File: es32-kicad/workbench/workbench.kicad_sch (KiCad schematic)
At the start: 67 parts, among them J1 GND|+5, J10 Rotary Encoder, J11 A[7..0], J2 [9..16], J3 B[0..7], J4 [17..24], J5 Conn_01x03_Socket, J6 Conn_01x03_Socket, J8 Conn_01x06_Socket, J9 [8..0]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

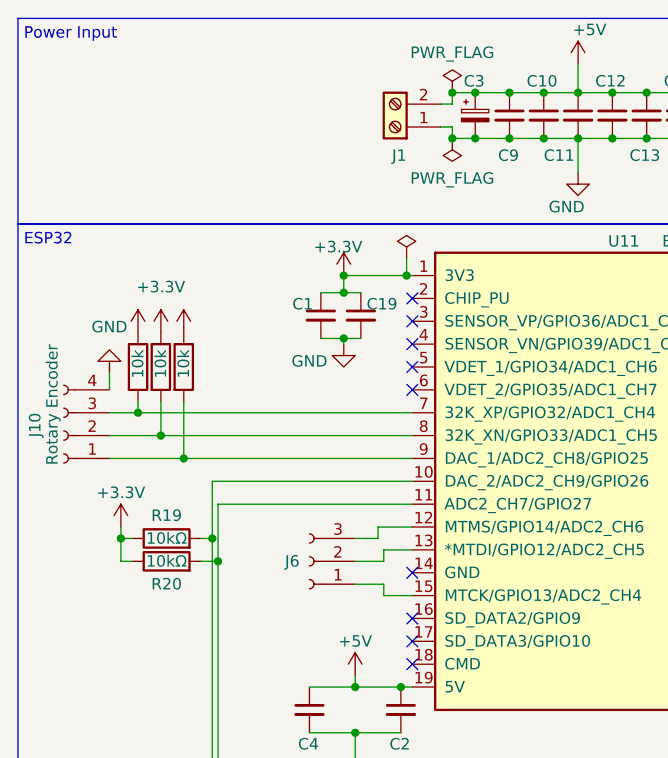
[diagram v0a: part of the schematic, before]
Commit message: adding pins for Leds. Silkscreen. logos. production files
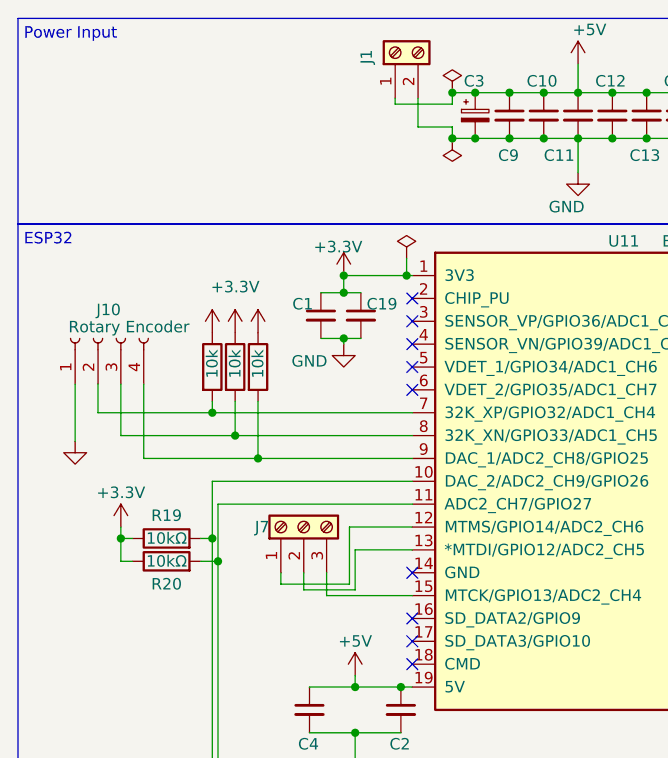
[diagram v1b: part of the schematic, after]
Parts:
- removed J6: Conn_01x03_Socket, Connector_PinHeader_2.54mm:PinHeader_1x03_P2.54mm_Vertical, symbol Connector:Conn_01x03_Socket
- added J7: Led-13-12-14, TerminalBlock_Phoenix:TerminalBlock_Phoenix_MKDS-3-3-5.08_1x03_P5.08mm_Horizontal, symbol Connector:Screw_Terminal_01x03
- H3: footprint MountingHole:MountingHole_4.3mm_M4_Pad_Via -> MountingHole:MountingHole_4.3mm_M4_DIN965_Pad
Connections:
- net +5V: now also J1.1 (Pin_1); no longer J1.2 (Pin_2)
- net GND: now also J1.2 (Pin_2), J10.1 (Pin_1); no longer J1.1 (Pin_1), J10.4 (Pin_4)
- net at U11.15 (MTCK/GPIO13/ADC2_CH4): now also J7.3 (Pin_3)
- net at U11.13 (*MTDI/GPIO12/ADC2_CH5): now also J7.2 (Pin_2)
- net at U11.12 (MTMS/GPIO14/ADC2_CH6): now also J7.1 (Pin_1)
- net at R35.2, U11.9 (DAC_1/ADC2_CH8/GPIO25): now also J10.4 (Pin_4); no longer J10.1 (Pin_1)
- net at R22.2, U11.8 (32K_XN/GPIO33/ADC1_CH5): now also J10.3 (Pin_3); no longer J10.2 (Pin_2)
- net at R21.2, U11.7 (32K_XP/GPIO32/ADC1_CH4): now also J10.2 (Pin_2); no longer J10.3 (Pin_3)
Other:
- moved on the sheet: J1, J10
